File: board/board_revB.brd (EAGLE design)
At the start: 94 x 44.5 mm, 90 parts, among them IC1 MCP1703CB, Q2 ULN2003AD, U1 MAX202, Y1 8Mhz

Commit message: [Board] working on rev B (full rework)
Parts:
- removed C34: 4.7uF, SparkFun-Passives:0603-CAP
- removed CON_AN, CON_KNK, CON_PWR, CON_RPM-VSS: (no value), SparkFun-Connectors:1X03_LOCK
- removed CON_CAN, CON_K-LINE, CON_UART1, CON_UART2: M02LOCK, SparkFun-Connectors:1X02_LOCK
- removed CON_USB: (no value), SparkFun-Connectors:1X04_LOCK
- removed D5: B240A, SparkFun-DiscreteSemi:SMA-DIODE
- removed IC1: MCP1703CB, linear:SOT23
- removed IC_FRAM: FM25L04B, microchip:SO-08
- removed IC_REG: LM1117-3.3, v-reg:DPACK
- removed R10, R25, R26: 1K, SparkFun-Resistors:0603-RES
- removed R14: 0R, SparkFun-Resistors:0603-RES
- removed TVS2: NUP4201MR6, misc:SOT23-6
- added C14: 10nF, SparkFun-Capacitors:0603-CAP
- added C9: 47uF 25v, SparkFun-Passives:CPOL-RADIAL-10UF-25V
- added F2: 1206L020 24V 0.2A, misc:PTC-1206
- added IC_EE: FM25L04B, microchip:SO-08
- added JP1: USBSMD, SparkFun-Connectors:USB-MINIB
- added U2, U3: LDK120DM33R, SparkFun-PowerIC:SOT23-5
- added VR1: LM2931, SparkFun-PowerIC:SO08
- added X2: (no value), con-molex-micro-fit-3_0:43045-1600
- C1: value 4.7uF -> 1uF
- CON_DBG: value (none) -> JST_VERTICAL; device SparkFun-Connectors:2X3 -> SparkFun-Connectors:JST-6-SMD-VERT-1.0MM
- D1: value B240A -> BAT165; device SparkFun-DiscreteSemi:SMA-DIODE -> SparkFun-DiscreteSemi:SOD-323
- D6: value B240A -> BAT165
- F1: value 24V 0.75A -> 1206L020 24V 0.2A; device misc:C1812K -> misc:PTC-1206
- IC_OPA: value TL974IPW -> MCP6004
- R19, R20, R24: value 10K 1% -> 2K 1%
- R21, R22: value 56R -> 1K
- R23, R6, R7: value 10K 1% -> 1K 1%
- S1: value EG1213 -> (none); device adafruit:EG1213 -> SparkFun-Electromechanical:TACTILE_SWITCH_TALL
- moved C1 82.4 mm to (16.5, 3.00), turned to 90 degrees
- moved TP3 81.6 mm to (1.75, 9.50), flipped to the top
- moved F1 79.5 mm to (11.8, 4.75)
- moved D1 74.6 mm to (9.16, 7.86), turned to 90 degrees
- moved CON_DBG 65.7 mm to (80.5, 42.0), flipped to the top
- moved TVS1 64.0 mm to (11.8, 2.00)
- moved C2 57.1 mm to (30.8, 2.37), flipped to the top, turned to 90 degrees
- moved U$6 44.8 mm to (9.51, -16.7)
- moved C7 44.1 mm to (60.2, 7.75), flipped to the top, turned to 0 degrees
- moved C5 39.8 mm to (68.8, 7.75), flipped to the top, turned to 180 degrees
- moved Y1 39.8 mm to (64.5, 11.2), flipped to the top, turned to 180 degrees
- moved Q2 39.6 mm to (25.9, 15.8), flipped to the top, turned to 90 degrees
- moved C13 39.5 mm to (28.0, 39.0), flipped to the top, turned to 180 degrees
- moved C10 31.8 mm to (23.8, 39.2), flipped to the top, turned to 180 degrees
- moved C12 31.6 mm to (20.0, 37.2), flipped to the top, turned to 270 degrees
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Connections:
- removed net N$1: CON_KNK.2, R1.1
- removed net N$12: CON_RPM-VSS.3, R25.1
- removed net N$14: C5.2, R14.1, Y1.1
- removed net N$16: Q2.6, R25.2
- removed net N$18: C3.2, R10.1, R11.1
- removed net N$21: CON_RPM-VSS.2, R26.1
- removed net OP3_VINM: D4.3, R5.2, R8.1, STM32.28
- removed net OP3_VOUT: R5.1, STM32.27
- removed net SWDAT: CON_DBG.6, STM32.46
- removed net UART2_RXD_OUT: CON_UART2.2, U1.13
- removed net UART2_TXD_OUT: CON_UART2.1, U1.14
- removed net UART3_RXD_OUT: CON_UART1.2, U1.8
- removed net UART3_TXD_OUT: CON_UART1.1, U1.7
- removed net USART2_RX: STM32.56, U1.12
- removed net USART2_TX: STM32.55, U1.11
- removed net USART3_RX: STM32.52, U1.9
- removed net USART3_TX: STM32.51, U1.10
- new net AN2_IN: R32.1, X2.P$8
- new net AN3_IN: R4.1, X2.P$7
- new net FREQ1_RAW: Q2.6, X2.P$4
- new net FREQ2_RAW: Q2.7, X2.P$12
- new net KNK_AN: IC_OPA.14, R5.1, STM32.27
- new net KNK_BIAS: R1.1, X2.P$10
- new net KNK_IN: C4.1, X2.P$11
- new net N$32: C1.2, TVS1.A, VR1.6, VR1.7
- new net SWDIO: CON_DBG.4, STM32.46
- new net SWO: CON_DBG.6
- new net UART1_RXD_232: U1.13, X2.P$2
- new net UART1_TXD_232: U1.14, X2.P$3
- new net UART2_RX: STM32.56, U1.9
- new net UART2_RXD_232: U1.8
- new net UART2_TX: STM32.55, U1.10
- new net UART2_TXD_232: U1.7
- new net UART3_RX: IC_KLINE.1, R2.1, STM32.52
- new net UART3_TX: IC_KLINE.4, STM32.51
- new net VDDA: C30.1, C31.1, STM32.13, U3.5
- net +12V: now also D1.2, X2.P$16; no longer CON_PWR.3, D1.A
- net +3V3: now also IC_EE.3, IC_EE.7, IC_EE.8, S1.B2, U2.5; no longer C13.1, C2.1, C30.1, C31.1, C34.1, IC_FRAM.3, IC_FRAM.7, IC_FRAM.8, IC_REG.4, LED1.A, LED2.A, R1.2, STM32.13, TP2.P$1, U1.16
- net +5V: now also C13.1, C2.1, C9.1, LED1.A, LED2.A, R1.2, TP2.P$1, U1.16, U2.1, U2.3, U3.1, U3.3, VR1.1; no longer IC1.2
- net AN2: now also STM32.10; no longer STM32.11
- net AN3: now also STM32.11; no longer STM32.10
- net BOOT0: now also S1.A2
- net BUT1: now also S2.2; no longer S1.2
- net BUT2: no longer S2.2
- net CANH: now also X2.P$6; no longer CON_CAN.2
- net CANL: now also X2.P$5; no longer CON_CAN.1
- net DAC1: now also IC_OPA.12
- net GND: now also C14.2, C9.2, CON_DBG.3, IC_EE.4, JP1.GND, U2.2, U3.2, VR1.2, VR1.3, X2.P$1, X2.P$15, X2.P$9; no longer C1.2, C34.2, CON_AN.1, CON_DBG.4, CON_KNK.1, CON_PWR.2, CON_RPM-VSS.1, CON_USB.4, IC1.1, IC_FRAM.4, IC_OPA.12, IC_OPA.13, IC_REG.1, S1.3, TVS1.A, TVS2.2
- net K-LINE: now also X2.P$14; no longer CON_K-LINE.2
- net N$17: now also JP1.D-; no longer CON_USB.2, TVS2.4
- net N$2: now also STM32.28; no longer CON_AN.3, R32.1
- net N$3: now also F2.1, Q2.16; no longer CON_AN.2, R4.1
- net N$4: now also D4.3, IC_OPA.13, R5.2, R8.1; no longer C4.1, CON_KNK.3
- net N$7: now also JP1.D+; no longer CON_USB.1, TVS2.3
- net N$9: now also C14.1, U3.4; no longer Q2.7, R26.2
- net NRST: now also C3.2, CON_DBG.5, R11.1; no longer CON_DBG.3, R10.2
- net OSC_OUT: now also C5.2, Y1.1; no longer R14.2
- net RELAY_OUT: now also F2.2; no longer CON_PWR.1, Q2.16
- net SCS: now also X2.P$13; no longer CON_K-LINE.1
- net SPI2_MISO: now also IC_EE.2; no longer IC_FRAM.2
- net SPI2_MOSI: now also IC_EE.5; no longer IC_FRAM.5
- net SPI2_NSS: now also IC_EE.1; no longer IC_FRAM.1
- net SPI2_SCK: now also IC_EE.6; no longer IC_FRAM.6
- net UART1_RX: now also U1.12; no longer IC_KLINE.1, R2.1
- net UART1_TX: now also U1.11; no longer IC_KLINE.4
- net USB_VBUS: now also JP1.VBUS; no longer CON_USB.3, D5.A, TVS2.5
- net VCC: now also D1.1; no longer D1.C, D5.C
- net VCC_PROT: now also VR1.8; no longer IC1.3, IC_REG.3
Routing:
- net +3V3: track 303.0 -> 0.00 mm, vias 15 -> 0
- net +12V: track 106.5 -> 0.00 mm, vias 2 -> 0
- net SCS: track 70.5 -> 0.00 mm
- net NRST: track 68.9 -> 0.00 mm, vias 1 -> 0
- net UART1_RX: track 68.6 -> 0.00 mm
- net VCC_PROT: track 67.1 -> 0.00 mm, vias 2 -> 0
- net UART1_TX: track 58.5 -> 0.00 mm
- net +5V: track 58.1 -> 0.00 mm
- net USB_DM: track 56.9 -> 0.00 mm, vias 2 -> 0
- net USB_DP: track 55.1 -> 0.00 mm, vias 2 -> 0
- net USB_CTRL: track 52.2 -> 0.00 mm, vias 2 -> 0
- net N$21: track 47.0 -> 0.00 mm, vias 1 -> 0
- net N$12: track 43.2 -> 0.00 mm, vias 1 -> 0
- net USB_VBUS: track 40.6 -> 0.00 mm, vias 2 -> 0
- net AN3: track 39.9 -> 0.00 mm
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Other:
- board text removed: "1"
- board text removed: "6"
- board text removed: "ANALOG"
- board text removed: "CAN"
- board text removed: "K-LINE"
- board text removed: "POWER"
- board text removed: "RPM/SPD"
- board text removed: "UART2"
- board text removed: "UART3"

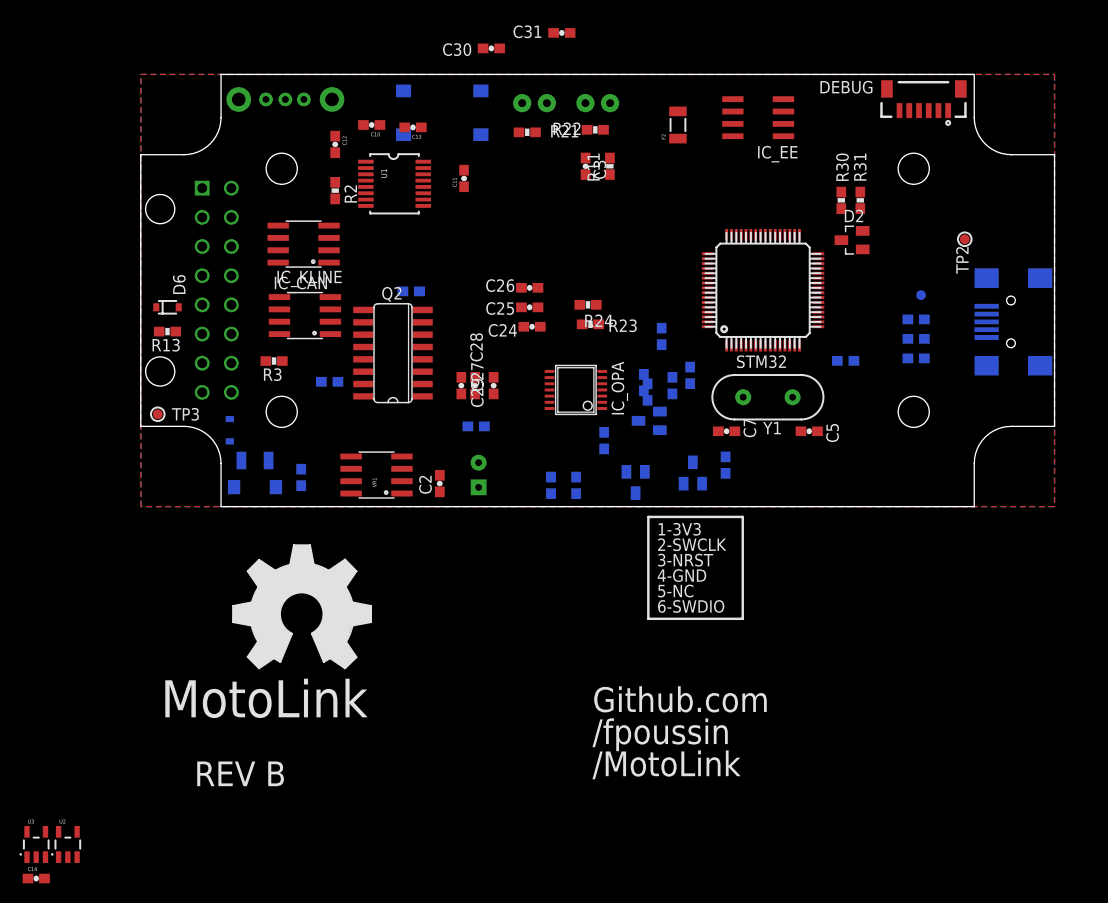
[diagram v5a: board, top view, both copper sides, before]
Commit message: [Board] working on rev B (routing)
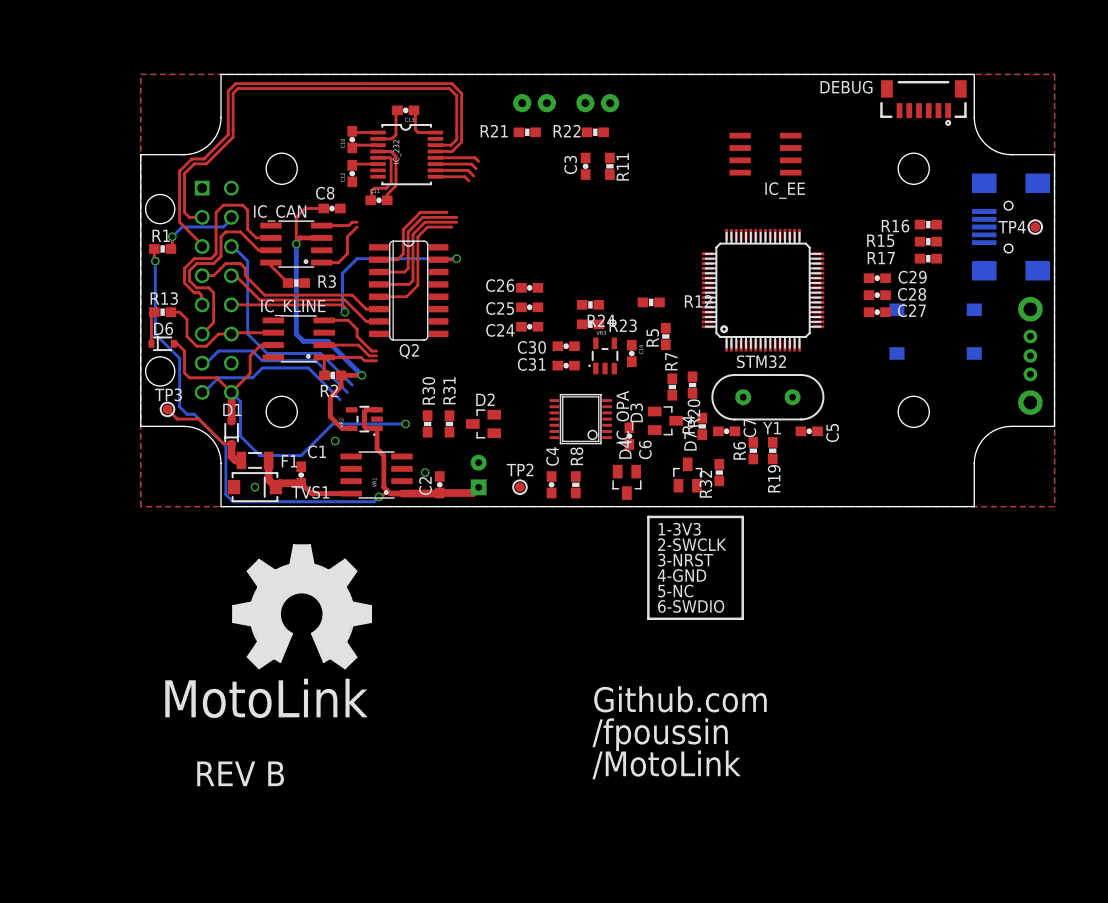
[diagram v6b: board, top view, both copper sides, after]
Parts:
- removed F2: 1206L020 24V 0.2A, misc:PTC-1206
- removed U1: MAX202, SparkFun-DigitalIC:TSSOP16
- removed U2, U3: LDK120DM33R, SparkFun-PowerIC:SOT23-5
- added IC_232: MAX202, SparkFun-DigitalIC:TSSOP16
- added VR2, VR3: LDK120DM33R, SparkFun-PowerIC:SOT23-5
- moved C14 81.7 mm to (50.5, 15.8), turned to 270 degrees
- moved S2 81.0 mm to (91.5, 15.5), turned to 270 degrees
- moved S1 55.5 mm to (81.8, 18.0), turned to 0 degrees
- moved TP2 52.4 mm to (39.0, 2.00)
- moved R30 48.4 mm to (29.5, 8.50)
- moved R31 48.1 mm to (31.8, 8.50)
- moved C27 43.4 mm to (75.8, 20.0), turned to 0 degrees
- moved C28 42.4 mm to (75.8, 21.8), turned to 0 degrees
- moved D2 42.4 mm to (35.2, 8.50)
- moved C29 41.0 mm to (75.8, 23.5), turned to 0 degrees
- moved R1 37.1 mm to (2.25, 26.5), flipped to the top
- moved C31 34.2 mm to (43.8, 14.5)
- moved C30 31.6 mm to (43.8, 16.5)
- moved R12 24.7 mm to (52.5, 21.0), flipped to the top, turned to 180 degrees
- moved C6 23.6 mm to (50.2, 7.25), flipped to the top, turned to 270 degrees
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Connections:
- removed net N$3: F2.1, Q2.16
- removed net N$32: C1.2, TVS1.A, VR1.6, VR1.7
- removed net RELAY_OUT: F2.2
- net +3V3: now also VR2.5; no longer U2.5
- net +5V: now also IC_232.16, VR2.1, VR2.3, VR3.1, VR3.3; no longer U1.16, U2.1, U2.3, U3.1, U3.3
- net GND: now also C1.2, IC_232.15, TVS1.A, VR1.6, VR1.7, VR2.2, VR3.2; no longer U1.15, U2.2, U3.2
- net N$20: now also IC_232.4; no longer U1.4
- net N$22: now also IC_232.5; no longer U1.5
- net N$23: now also IC_232.3; no longer U1.3
- net N$26: now also IC_232.1; no longer U1.1
- net N$27: now also IC_232.6; no longer U1.6
- net N$29: now also IC_232.2; no longer U1.2
- net N$9: now also VR3.4; no longer U3.4
- net RELAY_TRIG: no longer Q2.1
- net UART1_RX: now also IC_232.12; no longer U1.12
- net UART1_RXD_232: now also IC_232.13, X2.P$3; no longer U1.13, X2.P$2
- net UART1_TX: now also IC_232.11; no longer U1.11
- net UART1_TXD_232: now also IC_232.14, X2.P$2; no longer U1.14, X2.P$3
- net UART2_RX: now also IC_232.9; no longer U1.9
- net UART2_RXD_232: now also IC_232.8; no longer U1.8
- net UART2_TX: now also IC_232.10; no longer U1.10
- net UART2_TXD_232: now also IC_232.7; no longer U1.7
- net VDDA: now also VR3.5; no longer U3.5
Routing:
- net +5V: track 0.00 -> 71.2 mm, vias 0 -> 2
- net UART1_RXD_232: track 0.00 -> 52.6 mm
- net UART1_TXD_232: track 0.00 -> 47.5 mm
- net +12V: track 0.00 -> 43.8 mm, vias 0 -> 1
- net +3V3: track 0.00 -> 36.3 mm, vias 0 -> 2
- net SCS: track 0.00 -> 30.7 mm, vias 0 -> 2
- net KNK_IN: track 0.00 -> 22.7 mm
- net CANL: track 0.00 -> 21.4 mm
- net FREQ1_RAW: track 0.00 -> 21.1 mm
- net CANH: track 0.00 -> 20.7 mm
- net AN3_IN: track 0.00 -> 17.2 mm
- net FREQ2_RAW: track 0.00 -> 17.1 mm
- net AN2_IN: track 0.00 -> 16.6 mm
- net K-LINE: track 0.00 -> 13.6 mm
- net LED2_TRIG: track 0.00 -> 13.4 mm
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
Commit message: [Board] working on rev B (routing)
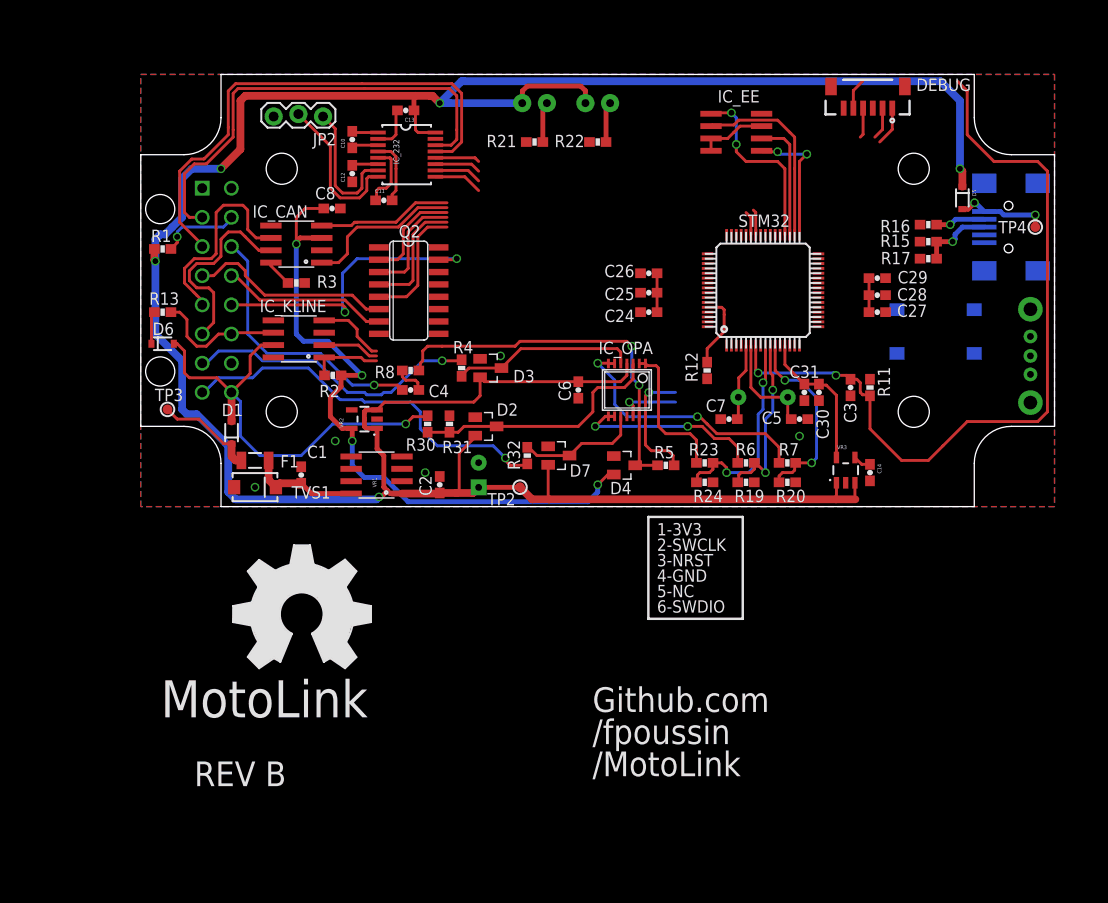
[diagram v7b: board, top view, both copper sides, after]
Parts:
- added D5: BAT165, SparkFun-DiscreteSemi:SOD-323
- added JP2: (no value), SparkFun-Connectors:1X03_LOCK
- moved C3 35.5 mm to (73.0, 12.2)
- moved R11 35.1 mm to (75.0, 12.2), turned to 90 degrees
- moved VR3 27.4 mm to (72.5, 3.75)
- moved C14 27.4 mm to (75.0, 3.50)
- moved C30 26.4 mm to (69.8, 11.8), turned to 270 degrees
- moved R4 25.5 mm to (33.0, 14.2), turned to 270 degrees
- moved C31 24.7 mm to (68.2, 11.8), turned to 270 degrees
- moved R24 21.7 mm to (58.0, 2.50)
- moved R8 20.7 mm to (27.8, 14.0), turned to 180 degrees
- moved R32 19.8 mm to (39.8, 5.25)
- moved D3 18.8 mm to (36.0, 14.2)
- moved R23 18.5 mm to (58.0, 4.50), turned to 0 degrees
- moved C4 17.5 mm to (27.8, 12.0), turned to 0 degrees
- moved R7 14.2 mm to (66.5, 4.50), turned to 180 degrees
- moved R20 14.0 mm to (66.5, 2.50), turned to 0 degrees
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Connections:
- net +5V: now also D5.1
- net GND: now also JP2.3
- net UART2_RXD_232: now also JP2.2
- net UART2_TXD_232: now also JP2.1
- net USB_VBUS: now also D5.2
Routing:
- net +5V: track 71.2 -> 280.6 mm, vias 2 -> 5
- net NRST: track 0.00 -> 84.7 mm, vias 0 -> 2
- net +3V3: track 36.3 -> 88.7 mm, vias 2 -> 4
- net N$4: track 0.00 -> 39.4 mm, vias 0 -> 2
- net AN3_N: track 0.00 -> 27.0 mm, vias 0 -> 2
- net N$24: track 0.00 -> 26.2 mm
- net AN2_IN: track 16.6 -> 39.8 mm, vias 0 -> 1
- net AN1: track 0.00 -> 21.4 mm, vias 0 -> 2
- net AN2_N: track 0.00 -> 20.2 mm, vias 0 -> 2
- net AN3: track 0.00 -> 19.8 mm, vias 0 -> 2
- net SPI2_SCK: track 0.00 -> 19.6 mm
- net N$5: track 0.00 -> 18.9 mm
- net SPI2_MOSI: track 0.00 -> 18.9 mm, vias 0 -> 2
- net AN2: track 0.00 -> 18.3 mm, vias 0 -> 2
- net UART2_RXD_232: track 0.00 -> 15.9 mm
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
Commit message: [Board] working on rev B (routing)
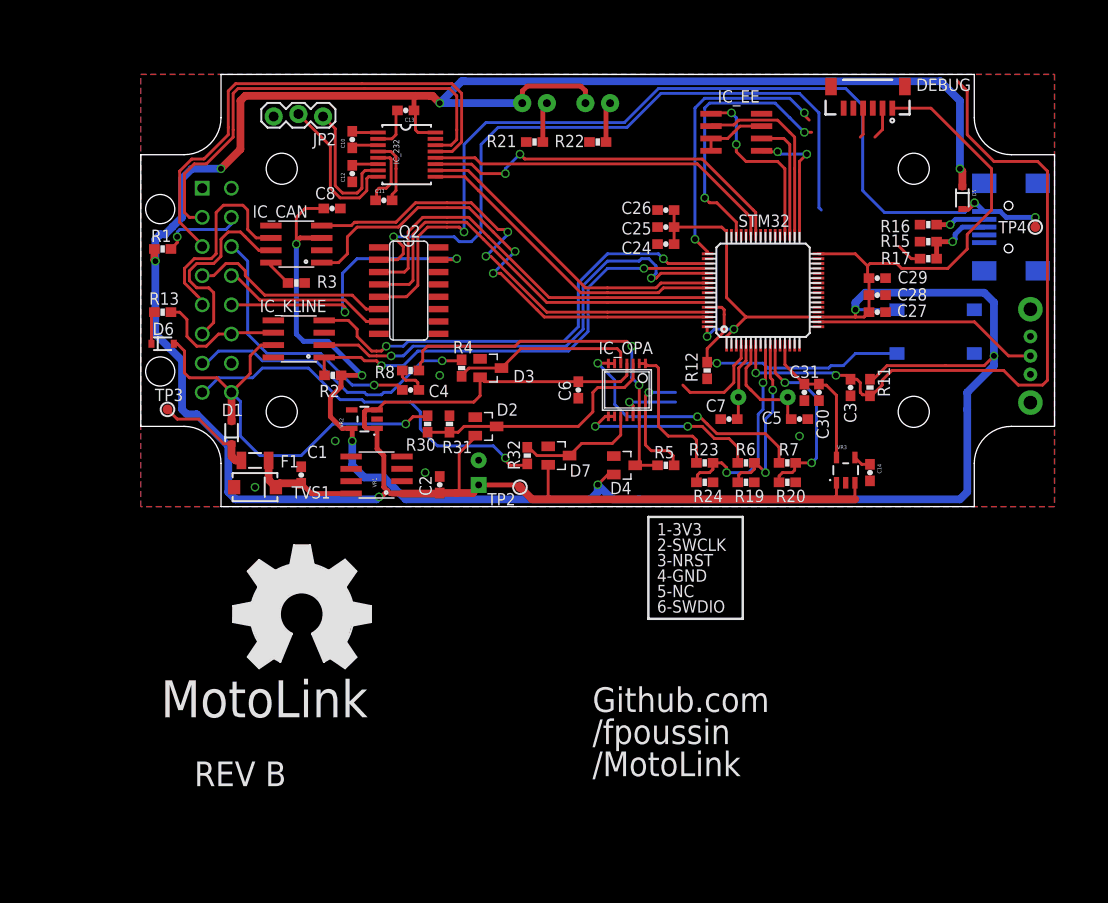
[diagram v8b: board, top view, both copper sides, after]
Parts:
- moved C24 7.22 mm to (54.0, 27.0)
- moved C25 6.97 mm to (54.0, 28.8)
- moved C26 6.73 mm to (54.0, 30.5)
- moved C9 0.25 mm to (34.8, 3.50)
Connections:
- net DAC2 renamed SPI1_SCK
- net RELAY_TRIG renamed SPI1_MOSI
- removed net BUT2: STM32.2
- removed net N$2: STM32.28
- new net SPI1_MISO: STM32.22
- net BUT1: now also STM32.18; no longer STM32.3
- net GND: no longer STM32.18
- net LED1_TRIG: now also STM32.58; no longer STM32.16
- net LED2_TRIG: now also STM32.59; no longer STM32.17
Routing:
- net +3V3: track 88.7 -> 254.4 mm, vias 4 -> 8
- net USB_VBUS: track 22.5 -> 99.0 mm, vias 2 -> 3
- net SCS_TRIG: track 10.5 -> 71.4 mm, vias 0 -> 1
- net KL-CS: track 5.85 -> 49.1 mm, vias 0 -> 2
- net UART3_TX: track 7.13 -> 48.4 mm, vias 0 -> 2
- net UART3_RX: track 7.39 -> 48.4 mm, vias 0 -> 2
- net CAN_RX: track 13.9 -> 50.0 mm, vias 0 -> 2
- net CAN_TX: track 16.3 -> 52.2 mm, vias 0 -> 2
- net UART1_TX: track 7.40 -> 39.3 mm, vias 0 -> 2
- net LED1_TRIG: track 11.5 -> 41.8 mm
- net LED2_TRIG: track 12.4 -> 42.7 mm
- net UART1_RX: track 7.11 -> 36.8 mm
- net SWCLK: track 3.31 -> 32.1 mm, vias 0 -> 2
- net UART2_TX: track 4.90 -> 33.2 mm
- net UART2_RX: track 5.04 -> 33.1 mm
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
